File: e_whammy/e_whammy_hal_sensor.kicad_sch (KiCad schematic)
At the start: 9 parts, among them J1 I/O connector, U1 HT7550-1, U2 DRV5056

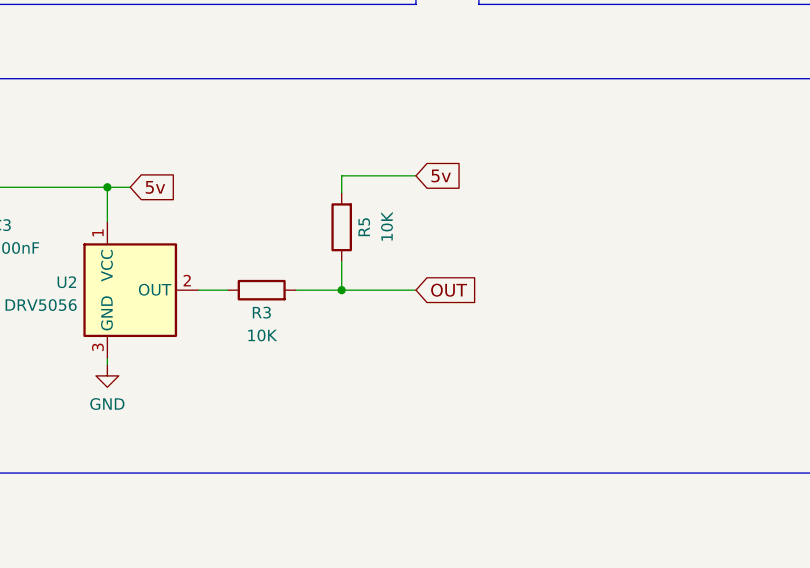
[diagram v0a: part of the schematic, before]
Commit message: Updated circuit matching the E-Whammy control design.
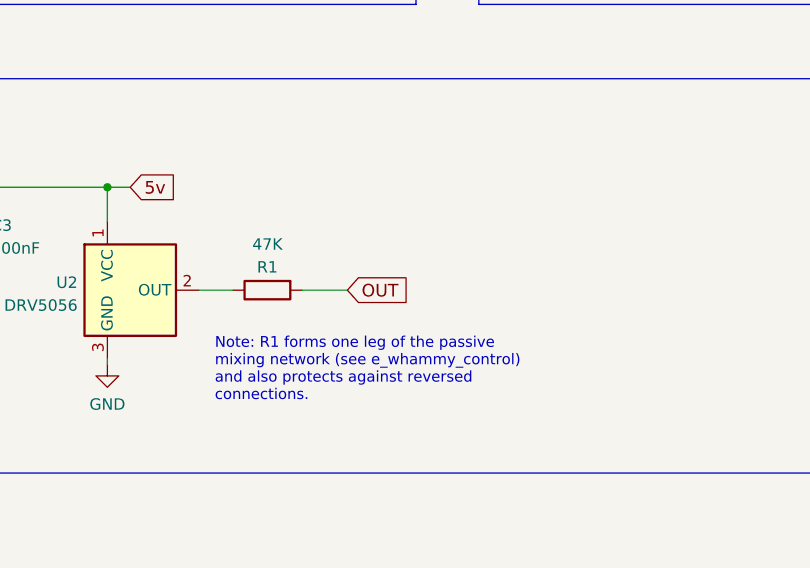
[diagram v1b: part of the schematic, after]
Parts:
- removed R3, R5: 10K, Resistor_SMD:R_0402_1005Metric, symbol Device:R
- added R1: 47K, Resistor_SMD:R_0402_1005Metric, symbol Device:R
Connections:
- net OUT: now also R1.2
- net at U2.2 (OUT): now also R1.1
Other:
- note added: "Note: R1 forms one leg of the passive mixing network (see e_whammy_control) and also protects against reversed connections."
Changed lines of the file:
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@@
+		)
+	)
+	(text "Note: R1 forms one leg of the passive \nmixing network (see e_whammy_control) \nand also protects against reversed \nconnections."
+		(exclude_from_sim no)
+		(at 142.748 127 0)
+		(effects
+			(font
+				(size 1.2 1.2)
+			)
+			(justify left)
 		)
 	)
@@
 	)
 	(junction
-		(at 156.845 118.11)
-		(diameter 0)
-		(color 0 0 0 0)
-	)
-	(junction
 		(at 115.57 58.42)
 		(diameter 0)
@@
 	(wire
 		(pts
-			(xy 156.845 114.935) (xy 156.845 118.11)
-		)
-		(stroke
-			(width 0)
-			(type default)
-		)
-	)
-	(wire
-		(pts
 			(xy 115.57 58.42) (xy 119.38 58.42)
 		)
@@
 	(wire
 		(pts
-			(xy 156.845 107.315) (xy 156.845 105.41)
-		)
-		(stroke
-			(width 0)
-			(type default)
-		)
-	)
-	(wire
-		(pts
 			(xy 115.57 106.68) (xy 130.81 106.68)
 		)
@@
 	(wire
 		(pts
-			(xy 140.97 118.11) (xy 144.145 118.11)
-		)
-		(stroke
-			(width 0)
-			(type default)
-		)
-	)
-	(wire
-		(pts
-			(xy 156.845 105.41) (xy 165.1 105.41)
-		)
-		(stroke
-			(width 0)
-			(type default)
-		)
-	)
-	(wire
-		(pts
-			(xy 156.845 118.11) (xy 165.1 118.11)
+			(xy 140.97 118.11) (xy 144.78 118.11)
 		)
 		(stroke
@@
 	(wire
 		(pts
-			(xy 151.765 118.11) (xy 156.845 118.11)
+			(xy 152.4 118.11) (xy 157.48 118.11)
 		)
 		(stroke
@@
 	(global_label "5v"
 		(shape input)
-		(at 165.1 105.41 0)
+		(at 144.78 58.42 0)
 		(fields_autoplaced yes)
 		(effects
@@
 		)
 		(property "Intersheetrefs" "${INTERSHEET_REFS}"
-			(at 170.5015 105.3148 0)
+			(at 150.1815 58.3248 0)
 			(effects
 				(font
@@
 		)
 	)
-	(global_label "5v"
+	(global_label "OUT"
 		(shape input)
-		(at 144.78 58.42 0)
+		(at 157.48 118.11 0)
 		(fields_autoplaced yes)
 		(effects
@@
 		)
 		(property "Intersheetrefs" "${INTERSHEET_REFS}"
-			(at 150.1815 58.3248 0)
+			(at 164.6232 118.0148 0)
 			(effects
 				(font
@@
 		)
 	)
-	(global_label "OUT"
+	(global_label "V+"
 		(shape input)
-		(at 165.1 118.11 0)
+		(at 102.87 58.42 180)
 		(fields_autoplaced yes)
 		(effects
@@
 				(size 1.4 1.4)
 			)
-			(justify left)
-		)
-		(property "Intersheetrefs" "${INTERSHEET_REFS}"
-			(at 172.2432 118.0148 0)
-			(effects
-				(font
-					(size 1.524 1.524)
-				)
-				(justify left)
-				(hide yes)
-			)
-		)
-	)
-	(global_label "V+"
-		(shape input)
-		(at 102.87 58.42 180)
-		(fields_autoplaced yes)
-		(effects
-			(font
-				(size 1.4 1.4)
-			)
 			(justify right)
 		)
@@
 				(justify right)
 				(hide yes)
-			)
-		)
-	)
-	(symbol
-		(lib_id "Device:R")
-		(at 147.955 118.11 90)
-		(unit 1)
-		(exclude_from_sim no)
-		(in_bom yes)
-		(on_board yes)
-		(dnp no)
-		(property "Reference" "R3"
-			(at 147.955 120.6531 90)
-			(effects
-				(font
-					(size 1.27 1.27)
-				)
-			)
-		)
-		(property "Value" "10K"
-			(at 147.955 123.19 90)
-			(effects
-				(font
-					(size 1.27 1.27)
-				)
-			)
-		)
-		(property "Footprint" "Resistor_SMD:R_0402_1005Metric"
-			(at 147.955 119.888 90)
-			(effects
-				(font
-					(size 1.27 1.27)
-				)
-				(hide yes)
-			)
-		)
-		(property "Datasheet" "~"
-			(at 147.955 118.11 0)
-			(effects
-				(font
-					(size 1.27 1.27)
-				)
-				(hide yes)
-			)
-		)
-		(property "Description" "Resistor"
-			(at 147.955 118.11 0)
-			(effects
-				(font
-					(size 1.27 1.27)
-				)
-				(hide yes)
-			)
-		)
-		(property "LCSC" "C25744"
-			(at 147.955 118.11 0)
-			(effects
-				(font
-					(size 1.524 1.524)
-				)
-				(hide yes)
-			)
-		)
-		(pin "1"
-		)
-		(pin "2"
-		)
-		(instances
-			(project ""
-				(path "/e63e39d7-6ac0-4ffd-8aa3-1841a4541b55"
-					(reference "R3")
-					(unit 1)
-				)
 			)
 		)
@@
 	(symbol
 		(lib_id "Device:R")
-		(at 156.845 111.125 180)
+		(at 148.59 118.11 90)
+		(mirror x)
 		(unit 1)
 		(exclude_from_sim no)
@@
 		(on_board yes)
 		(dnp no)
-		(property "Reference" "R5"
-			(at 159.3881 111.125 90)
-			(effects
-				(font
-					(size 1.27 1.27)
-				)
-			)
-		)
-		(property "Value" "10K"
-			(at 161.925 111.125 90)
+		(property "Reference" "R1"
+			(at 148.59 115.5669 90)
+			(effects
+				(font
+					(size 1.27 1.27)
+				)
+			)
+		)
+		(property "Value" "47K"
+			(at 148.59 113.03 90)
 			(effects
 				(font
@@
 		)
 		(property "Footprint" "Resistor_SMD:R_0402_1005Metric"
-			(at 158.623 111.125 90)
+			(at 148.59 116.332 90)
 			(effects
 				(font
@@
 		)
 		(property "Datasheet" "~"
-			(at 156.845 111.125 0)
+			(at 148.59 118.11 0)
 			(effects
 				(font
@@
 		)
 		(property "Description" "Resistor"
-			(at 156.845 111.125 0)
-			(effects
-				(font
-					(size 1.27 1.27)
-				)
-				(hide yes)
-			)
-		)
-		(property "LCSC" "C25744"
-			(at 156.845 111.125 0)
+			(at 148.59 118.11 0)
+			(effects
+				(font
+					(size 1.27 1.27)
+				)
+				(hide yes)
+			)
+		)
+		(property "LCSC" "C25792"
+			(at 148.59 118.11 0)
 			(effects
 				(font
@@
 		)
 		(instances
-			(project ""
+			(project "e_whammy_hal_sensor"
 				(path "/e63e39d7-6ac0-4ffd-8aa3-1841a4541b55"
-					(reference "R5")
+					(reference "R1")
 					(unit 1)
 				)

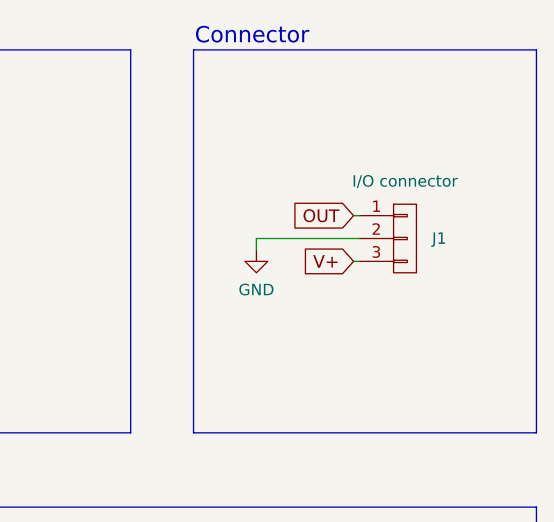
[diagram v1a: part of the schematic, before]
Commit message: E-Whammy update: bug fixes and refinements
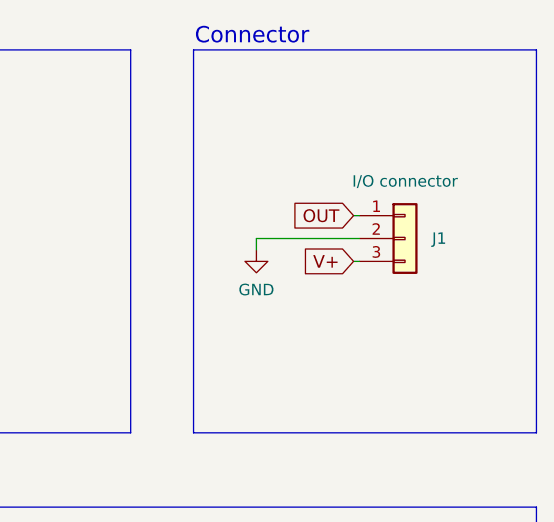
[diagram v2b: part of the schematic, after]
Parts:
- J1: symbol cycfi_library:conn_1x3 -> Connector_Generic:Conn_01x03
- U1: footprint Package_TO_SOT_SMD:SOT-23 -> cycfi_library:SOT-23-132; LCSC C16106 -> C5379082
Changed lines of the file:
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@@
 		(title "E-Whammy HAL Effect Sensor")
 		(date "2025-07-18")
-		(rev "v1.0")
+		(rev "v1.1")
 		(company "Document Number: 2025005")
 	)
@@
 			)
 		)
-		(property "Footprint" "Package_TO_SOT_SMD:SOT-23"
+		(property "Footprint" "cycfi_library:SOT-23-132"
 			(at 127 53.34 0)
 			(effects
@@
 			)
 		)
-		(property "LCSC" "C16106"
+		(property "LCSC" "C5379082"
 			(at 127 58.42 0)
 			(effects
@@
 	)
 	(symbol
-		(lib_id "cycfi_library:conn_1x3")
+		(lib_id "Connector_Generic:Conn_01x03")
 		(at 195.58 64.77 0)
 		(unit 1)
@@
 			)
 		)
-		(property "Datasheet" ""
+		(property "Datasheet" "~"
 			(at 195.58 64.77 0)
 			(effects
@@
 			)
 		)
-		(property "Description" ""
+		(property "Description" "Generic connector, single row, 01x03, script generated (kicad-library-utils/schlib/autogen/connector/)"
 			(at 195.58 64.77 0)
 			(effects
